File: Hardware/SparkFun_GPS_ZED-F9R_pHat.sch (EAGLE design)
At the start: 87 parts, among them J1 QWIIC_RIGHT_ANGLE, J2 RASPBERRYPI-40-PIN-GPIO_SMD_S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, J4 U.FL, U1 UBLOX_ZED_F9R, U2 HCPL-270L

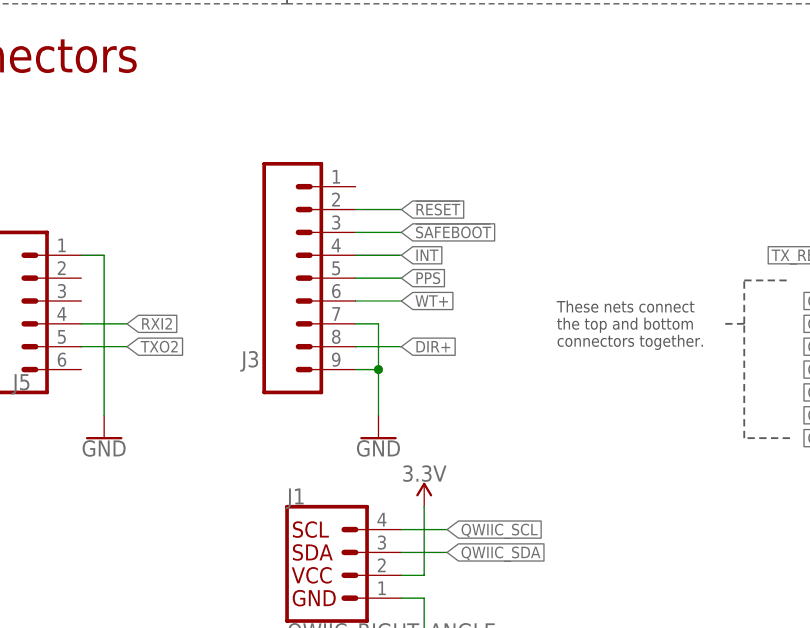
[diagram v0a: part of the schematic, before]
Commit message: Replaces 9-pin connector with 8-pin
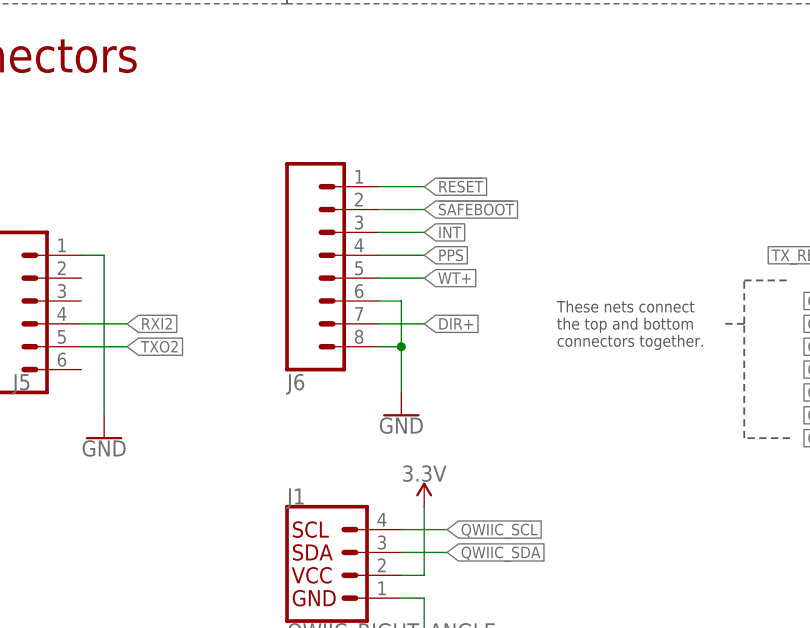
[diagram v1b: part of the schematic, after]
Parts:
- removed J3: (no value), SparkFun-Connectors:CONN_09NO_SILK
- added J6: (no value), SparkFun-Connectors:CONN_08NO_SILK_FEMALE_PTH
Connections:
- net !RESET: now also J6.1; no longer J3.2
- net !SAFEBOOT: now also J6.2; no longer J3.3
- net DIR+: now also J6.7; no longer J3.8
- net GND: now also J6.6, J6.8; no longer J3.7, J3.9
- net INT: now also J6.3; no longer J3.4
- net PPS: now also J6.4; no longer J3.5
- net WT+: now also J6.5; no longer J3.6
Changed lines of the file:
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@@
 <part name="GND3" library="SparkFun-PowerSymbols" deviceset="GND" device=""/>
 <part name="SUPPLY4" library="SparkFun-PowerSymbols" deviceset="3.3V" device=""/>
-<part name="J3" library="SparkFun-Connectors" deviceset="CONN_09" device="NO_SILK"/>
 <part name="J5" library="SparkFun-Connectors" deviceset="CONN_06" device="NO_SILK_NO_POP"/>
 <part name="GND5" library="SparkFun-PowerSymbols" deviceset="GND" device=""/>
@@
 <part name="GND15" library="SparkFun-PowerSymbols" deviceset="GND" device=""/>
 <part name="GND22" library="SparkFun-PowerSymbols" deviceset="GND" device=""/>
-<part name="GND23" library="SparkFun-PowerSymbols" deviceset="GND" device=""/>
+<part name="GND24" library="SparkFun-PowerSymbols" deviceset="GND" device=""/>
+<part name="J6" library="SparkFun-Connectors" deviceset="CONN_08" device="NO_SILK_FEMALE_PTH"/>
 </parts>
 <sheets>
@@
 <attribute name="VALUE" x="312.42" y="81.534" size="1.778" layer="96" align="bottom-center"/>
 </instance>
-<instance part="J3" gate="J1" x="294.64" y="104.14" smashed="yes" rot="MR180">
-<attribute name="VALUE" x="292.1" y="114.046" size="1.778" layer="96" font="vector" rot="MR180"/>
-<attribute name="NAME" x="292.1" y="96.012" size="1.778" layer="95" font="vector" rot="MR180"/>
-</instance>
 <instance part="J5" gate="G$1" x="269.24" y="101.6" smashed="yes" rot="MR180">
 <attribute name="VALUE" x="266.7" y="111.506" size="1.778" layer="96" font="vector" rot="MR180"/>
@@
 <attribute name="VALUE" x="340.36" y="210.566" size="1.778" layer="96" align="top-center"/>
 </instance>
-<instance part="GND23" gate="1" x="307.34" y="86.36" smashed="yes">
-<attribute name="VALUE" x="307.34" y="86.106" size="1.778" layer="96" align="top-center"/>
+<instance part="GND24" gate="1" x="309.88" y="88.9" smashed="yes">
+<attribute name="VALUE" x="309.88" y="88.646" size="1.778" layer="96" align="top-center"/>
+</instance>
+<instance part="J6" gate="G$1" x="302.26" y="106.68" smashed="yes" rot="MR180">
+<attribute name="VALUE" x="297.18" y="119.126" size="1.778" layer="96" font="vector" rot="MR180"/>
+<attribute name="NAME" x="297.18" y="93.472" size="1.778" layer="95" font="vector" rot="MR180"/>
 </instance>
 </instances>
@@
 </segment>
 <segment>
-<pinref part="J3" gate="J1" pin="9"/>
-<wire x1="304.8" y1="93.98" x2="307.34" y2="93.98" width="0.1524" layer="91"/>
-<pinref part="GND23" gate="1" pin="GND"/>
-<wire x1="307.34" y1="88.9" x2="307.34" y2="93.98" width="0.1524" layer="91"/>
-<pinref part="J3" gate="J1" pin="7"/>
-<wire x1="304.8" y1="99.06" x2="307.34" y2="99.06" width="0.1524" layer="91"/>
-<wire x1="307.34" y1="93.98" x2="307.34" y2="99.06" width="0.1524" layer="91"/>
-<junction x="307.34" y="93.98"/>
+<wire x1="307.34" y1="96.52" x2="309.88" y2="96.52" width="0.1524" layer="91"/>
+<pinref part="GND24" gate="1" pin="GND"/>
+<wire x1="309.88" y1="91.44" x2="309.88" y2="96.52" width="0.1524" layer="91"/>
+<wire x1="307.34" y1="101.6" x2="309.88" y2="101.6" width="0.1524" layer="91"/>
+<wire x1="309.88" y1="96.52" x2="309.88" y2="101.6" width="0.1524" layer="91"/>
+<junction x="309.88" y="96.52"/>
+<pinref part="J6" gate="G$1" pin="6"/>
+<pinref part="J6" gate="G$1" pin="8"/>
 </segment>
 </net>
@@
 </segment>
 <segment>
-<wire x1="304.8" y1="104.14" x2="309.88" y2="104.14" width="0.1524" layer="91"/>
-<label x="309.88" y="104.14" size="1.27" layer="95" font="vector" rot="MR180" xref="yes"/>
-<pinref part="J3" gate="J1" pin="5"/>
-</segment>
-<segment>
 <wire x1="111.76" y1="200.66" x2="114.3" y2="200.66" width="0.1524" layer="91"/>
 <label x="114.3" y="200.66" size="1.27" layer="95" font="vector" xref="yes"/>
 <pinref part="R24" gate="G$1" pin="2"/>
 </segment>
+<segment>
+<wire x1="307.34" y1="106.68" x2="312.42" y2="106.68" width="0.1524" layer="91"/>
+<label x="312.42" y="106.68" size="1.27" layer="95" font="vector" rot="MR180" xref="yes"/>
+<pinref part="J6" gate="G$1" pin="4"/>
+</segment>
 </net>
 <net name="!RESET" class="0">
@@
 </segment>
 <segment>
-<wire x1="304.8" y1="111.76" x2="309.88" y2="111.76" width="0.1524" layer="91"/>
-<label x="309.88" y="111.76" size="1.27" layer="95" font="vector" rot="MR180" xref="yes"/>
-<pinref part="J3" gate="J1" pin="2"/>
+<wire x1="307.34" y1="114.3" x2="312.42" y2="114.3" width="0.1524" layer="91"/>
+<label x="312.42" y="114.3" size="1.27" layer="95" font="vector" rot="MR180" xref="yes"/>
+<pinref part="J6" gate="G$1" pin="1"/>
 </segment>
 </net>
@@
 </segment>
 <segment>
-<wire x1="304.8" y1="106.68" x2="309.88" y2="106.68" width="0.1524" layer="91"/>
-<label x="309.88" y="106.68" size="1.27" layer="95" font="vector" rot="MR180" xref="yes"/>
-<pinref part="J3" gate="J1" pin="4"/>
+<wire x1="307.34" y1="109.22" x2="312.42" y2="109.22" width="0.1524" layer="91"/>
+<label x="312.42" y="109.22" size="1.27" layer="95" font="vector" rot="MR180" xref="yes"/>
+<pinref part="J6" gate="G$1" pin="3"/>
 </segment>
 </net>
@@
 <net name="!SAFEBOOT" class="0">
 <segment>
-<wire x1="304.8" y1="109.22" x2="309.88" y2="109.22" width="0.1524" layer="91"/>
-<label x="309.88" y="109.22" size="1.27" layer="95" font="vector" rot="MR180" xref="yes"/>
-<pinref part="J3" gate="J1" pin="3"/>
-</segment>
-<segment>
 <wire x1="111.76" y1="198.12" x2="114.3" y2="198.12" width="0.1524" layer="91"/>
 <label x="114.3" y="198.12" size="1.27" layer="95" font="vector" xref="yes"/>
 <pinref part="R25" gate="G$1" pin="2"/>
+</segment>
+<segment>
+<wire x1="307.34" y1="111.76" x2="312.42" y2="111.76" width="0.1524" layer="91"/>
+<label x="312.42" y="111.76" size="1.27" layer="95" font="vector" rot="MR180" xref="yes"/>
+<pinref part="J6" gate="G$1" pin="2"/>
 </segment>
 </net>
@@
 </segment>
 <segment>
-<pinref part="J3" gate="J1" pin="6"/>
-<wire x1="304.8" y1="101.6" x2="309.88" y2="101.6" width="0.1524" layer="91"/>
-<label x="309.88" y="101.6" size="1.27" layer="95" font="vector" xref="yes"/>
+<wire x1="307.34" y1="104.14" x2="312.42" y2="104.14" width="0.1524" layer="91"/>
+<label x="312.42" y="104.14" size="1.27" layer="95" font="vector" xref="yes"/>
+<pinref part="J6" gate="G$1" pin="5"/>
 </segment>
 </net>
@@
 </segment>
 <segment>
-<pinref part="J3" gate="J1" pin="8"/>
-<wire x1="304.8" y1="96.52" x2="309.88" y2="96.52" width="0.1524" layer="91"/>
-<label x="309.88" y="96.52" size="1.27" layer="95" xref="yes"/>
-</segment>
-</net>
+<wire x1="307.34" y1="99.06" x2="312.42" y2="99.06" width="0.1524" layer="91"/>
+<label x="312.42" y="99.06" size="1.27" layer="95" xref="yes"/>
+<pinref part="J6" gate="G$1" pin="7"/>
+</segment>
+</net>

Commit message: Renumbers parts, adds PROD_ID for new parts
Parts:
- removed C9: 0.1uF, SparkFun-Capacitors:0.1UF-0402-6.3V-10%-X7R
- removed J8: (no value), SparkFun-Connectors:USB_C_2-LAYER
- removed PPS, PWR: JUMPER-SMT_2_NC_TRACE_SILK, SparkFun-Jumpers:JUMPER-SMT_2_NC_TRACE_SILK
- added C4: 0.1uF, SparkFun-Capacitors:0.1UF-0402-6.3V-10%-X7R
- added J3: (no value), SparkFun-Connectors:CONN_06NO_SILK_NO_POP
- added JP5: JUMPER-SMT_2_NO_SILK, SparkFun-Jumpers:JUMPER-SMT_2_NO_SILK
- added JP6: JUMPER-SMT_3_2-NC_TRACE_SILK, SparkFun-Jumpers:JUMPER-SMT_3_2-NC_TRACE_SILK
- C1: value 47pF -> 1.0uF; device SparkFun-Capacitors:47PF-0402-25V-5%-X7R -> SparkFun-Capacitors:1.0UF-0402-16V-10%
- C2: value 1nF -> 1.0uF; device SparkFun-Capacitors:1.0NF/1000PF-0402-25V-10%-X7R -> SparkFun-Capacitors:1.0UF-0402-16V-10%
- C3: value 1.0uF -> 47pF; device SparkFun-Capacitors:1.0UF-0402-16V-10% -> SparkFun-Capacitors:47PF-0402-25V-5%-X7R
- C6: value 1.0uF -> 1nF; device SparkFun-Capacitors:1.0UF-0402-16V-10% -> SparkFun-Capacitors:1.0NF/1000PF-0402-25V-10%-X7R
- D1: value 0.5A/40V/420mV -> RED; device SparkFun-DiscreteSemi:DIODE-SCHOTTKY-PMEG4005EJ -> SparkFun-LED:LED-RED0603
- D2: value RED -> BLUE; device SparkFun-LED:LED-RED0603 -> SparkFun-LED:LED-BLUE0603
- D4: value PRTR5V0U2F -> BLUE; device SparkFun-IC-Power:PRTR5V0U2F -> SparkFun-LED:LED-BLUE0603
- D5: value BLUE -> 0.5A/40V/420mV; device SparkFun-LED:LED-BLUE0603 -> SparkFun-DiscreteSemi:DIODE-SCHOTTKY-PMEG4005EJ
- D6: value BLUE -> PRTR5V0U2F; device SparkFun-LED:LED-BLUE0603 -> SparkFun-IC-Power:PRTR5V0U2F
- J1: value QWIIC_RIGHT_ANGLE -> U.FL; device SparkFun-Connectors:QWIIC_CONNECTORJS-1MM -> SparkFun-Connectors:U.FL2PIN
- J2: value RASPBERRYPI-40-PIN-GPIO_SMD_STACK_NOHOLES_NOREF -> (none); device SparkFun-Connectors:RASPBERRYPI-40-PIN-GPIO_SMD_STACK_NOHOLES_NOREF -> SparkFun-Connectors:USB_C_2-LAYER
- J4: value U.FL -> (none); device SparkFun-Connectors:U.FL2PIN -> SparkFun-Connectors:CONN_08NO_SILK_FEMALE_PTH
- J5: value (none) -> QWIIC_RIGHT_ANGLE; device SparkFun-Connectors:CONN_06NO_SILK_NO_POP -> SparkFun-Connectors:QWIIC_CONNECTORJS-1MM
- J6: value (none) -> RASPBERRYPI-40-PIN-GPIO_SMD_STACK_NOHOLES_NOREF; device SparkFun-Connectors:CONN_08NO_SILK_FEMALE_PTH -> SparkFun-Connectors:RASPBERRYPI-40-PIN-GPIO_SMD_STACK_NOHOLES_NOREF
- JP1: value JUMPER-SMT_2_NO_SILK -> JUMPER-SMT_2_NC_TRACE_SILK; device SparkFun-Jumpers:JUMPER-SMT_2_NO_SILK -> SparkFun-Jumpers:JUMPER-SMT_2_NC_TRACE_SILK
- JP2: value JUMPER-SMT_3_2-NC_TRACE_SILK -> JUMPER-SMT_2_NC_TRACE_SILK; device SparkFun-Jumpers:JUMPER-SMT_3_2-NC_TRACE_SILK -> SparkFun-Jumpers:JUMPER-SMT_2_NC_TRACE_SILK
- LOGO1: value SFE_LOGO_NAME_FLAME.2_INCH -> QWIIC_LOGO_5MM; device SparkFun-Aesthetics:SFE_LOGO_NAME_FLAME.2_INCH -> SparkFun-Aesthetics:QWIIC_LOGO_5MM
- LOGO3: value QWIIC_LOGO_5MM -> SFE_LOGO_NAME_FLAME.2_INCH; device SparkFun-Aesthetics:QWIIC_LOGO_5MM -> SparkFun-Aesthetics:SFE_LOGO_NAME_FLAME.2_INCH
- R1: value 3.3k -> 100K; device SparkFun-Resistors:3.3KOHM-0603-1/10W-1% -> SparkFun-Resistors:100KOHM-0402-1/16W-1%
- R12: value 100K -> 33; device SparkFun-Resistors:100KOHM-0402-1/16W-1% -> SparkFun-Resistors:33OHM-0603-1/10W-1%
- R13, R14, R2, R8: value 1k -> 33; device SparkFun-Resistors:1KOHM-0603-1/10W-1% -> SparkFun-Resistors:33OHM-0603-1/10W-1%
- R15, R16: value 5.1k -> 33; device SparkFun-Resistors:5.1KOHM-0402-1/16W-1% -> SparkFun-Resistors:33OHM-0603-1/10W-1%
- R18, R23: value 33 -> 2.2k; device SparkFun-Resistors:33OHM-0603-1/10W-1% -> SparkFun-Resistors:2.2KOHM-0603-1/10W-1%
- R19, R20, R22: value 33 -> 1k; device SparkFun-Resistors:33OHM-0603-1/10W-1% -> SparkFun-Resistors:1KOHM-0603-1/10W-1%
- R21: value 3.3k -> 1k; device SparkFun-Resistors:3.3KOHM-0603-1/10W-1% -> SparkFun-Resistors:1KOHM-0603-1/10W-1%
- R24, R25: value 33 -> 5.1k; device SparkFun-Resistors:33OHM-0603-1/10W-1% -> SparkFun-Resistors:5.1KOHM-0402-1/16W-1%
- R26, R29: value 33 -> 3.3k; device SparkFun-Resistors:33OHM-0603-1/10W-1% -> SparkFun-Resistors:3.3KOHM-0603-1/10W-1%
- R27, R28: value 33 -> 27; device SparkFun-Resistors:33OHM-0603-1/10W-1% -> SparkFun-Resistors:27OHM-0603-1/10W-1%
- R3, R4: value 2.2k -> 33; device SparkFun-Resistors:2.2KOHM-0603-1/10W-1% -> SparkFun-Resistors:33OHM-0603-1/10W-1%
- R30: value 470 -> 3.3k; device SparkFun-Resistors:470OHM-0603-1/10W-1% -> SparkFun-Resistors:3.3KOHM-0603-1/10W-1%
- R31: value 3.3k -> 910; device SparkFun-Resistors:3.3KOHM-0603-1/10W-1% -> classified:910OHM-0603-1/10W-5%
- R32: value 470 -> 910; device SparkFun-Resistors:470OHM-0603-1/10W-1% -> classified:910OHM-0603-1/10W-5%
- R33, R34: value 910 -> 470; device classified:910OHM-0603-1/10W-5% -> SparkFun-Resistors:470OHM-0603-1/10W-1%
- R6, R7: value 27 -> 33; device SparkFun-Resistors:27OHM-0603-1/10W-1% -> SparkFun-Resistors:33OHM-0603-1/10W-1%
- U2: value HCPL-270L -> HCPL-073L; device classified:HCPL-270L -> classified:HCPL-073L
- renumbered B1 to BT1, FD10 to FD2, FD11 to FD3, FD12 to FD4, FD9 to FD1, FRAME2 to FRAME1, GEO_STAT to JP4, H10 to H1, H11 to H3, H12 to H4, H9 to H2, RTK to JP3, U$30 to U3, U$31 to U4
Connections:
- net !RESET: now also J4.1, R5.2; no longer J6.1, R9.2
- net !SAFEBOOT: now also J4.2, R17.2; no longer J6.2, R25.2
- net 3.3V: now also C1.1, C2.1, C4.1, D5.A, J5.2, J6.3.3V, JP6.2, R1.2, R31.2, R32.2; no longer C3.1, C6.1, C9.1, D2.A, J1.2, J2.3.3V, JP2.2, R12.2, R33.2, R34.2
- net CE1: now also J6.CE1; no longer J2.CE1
- net DIR+: now also J4.7, R30.1; no longer J6.7, R31.1
- net DIR_IN: now also R33.2; no longer R32.2
- net DIR_OUT: now also R4.1; no longer R29.1
- net DIR_SCHMITT: now also R32.1; no longer R34.1
- net DMINUS: now also R28.2; no longer R7.2
- net DPLUS: now also R27.2; no longer R6.2
- net D_SEL: now also JP5.1; no longer JP1.1
- net GEOF_STAT: now also D4.A, R14.2; no longer D3.A, R22.2
- net GND: now also C4.2, D6.2, J1.GND, J3.1, J4.6, J4.8, J6.GND, JP1.1, JP2.1, JP5.2, R1.1, R24.1, R25.1; no longer C9.2, D4.2, J1.1, J4.GND, J6.6, J6.8, J8.GND, JP1.2, PPS.1, PWR.1, R12.1, R15.1, R16.1
- net GP12: now also J6.GP12; no longer J2.GP12
- net GP13: now also J6.GP13; no longer J2.GP13
- net GP16: now also J6.GP16; no longer J2.GP16
- net GP17: now also J6.GP17; no longer J2.GP17
- net GP18: now also J6.GP18#; no longer J2.GP18#
- net GP19: now also J6.GP19; no longer J2.GP19
- net GP20: now also J6.GP20; no longer J2.GP20
- net GP21: now also J6.GP21; no longer J2.GP21
- net GP22: now also J6.GP22; no longer J2.GP22
- net GP23: now also J6.GP23; no longer J2.GP23
- net GP24: now also J6.GP24; no longer J2.GP24
- net GP25: now also J6.GP25; no longer J2.GP25
- net GP26: now also J6.GP26; no longer J2.GP26
- net GP27: now also J6.GP27; no longer J2.GP27
- net GP4: now also J6.GP4; no longer J2.GP4
- net GP6: now also J6.GP6; no longer J2.GP6
- net ID_SC: now also J6.ID_SC; no longer J2.ID_SC
- net ID_SD: now also J6.ID_SD; no longer J2.ID_SD
- net INT: now also J4.3, R6.2; no longer J6.3, R10.2
- net N$1: now also JP6.1, R23.2; no longer JP2.1, R3.2
- net N$10: now also D6.5, J2.VBUS; no longer D4.5, J8.VBUS
- net N$11: now also D6.1, J2.D-; no longer D4.1, J8.D-
- net N$12: now also J2.CC2, R24.2; no longer J8.CC2, R15.2
- net N$13: now also R5.1; no longer R9.1
- net N$14: now also R6.1; no longer R10.1
- net N$15: now also R7.1; no longer R11.1
- net N$16: now also R22.1; no longer R8.1
- net N$17: now also D4.C, R22.2; no longer D3.C, R8.2
- net N$18: now also J2.CC1, R25.2; no longer J8.CC1, R16.2
- net N$19: now also R8.1; no longer R17.1
- net N$2: now also D5.C, R26.2; no longer D1.C, R1.2
- net N$20: now also R9.1; no longer R18.1
- net N$21: now also R10.1; no longer R19.1
- net N$22: now also R21.1; no longer R14.1
- net N$23: now also JP2.2, R20.1; no longer PPS.2, R13.1
- net N$24: now also D2.C, R20.2; no longer D5.C, R13.2
- net N$25: now also D3.C, R21.2; no longer D6.C, R14.2
- net N$26: now also R11.1; no longer R20.1
- net N$27: now also C6.1, D8.C, R29.2, R34.1; no longer C5.1, D7.C, R21.2, R30.1
- net N$28: now also R14.1; no longer R22.1
- net N$29: now also R15.1; no longer R23.1
- net N$3: now also JP6.3, R18.2; no longer JP2.3, R4.2
- net N$30: now also R16.1; no longer R24.1
- net N$31: now also R17.1; no longer R25.1
- net N$32: now also R12.1; no longer R26.1
- net N$33: now also R13.1; no longer R27.1
- net N$34: now also R3.2; no longer R28.2
- net N$35: now also R4.2; no longer R29.2
- net N$36: now also C5.1, D7.C, R30.2, R33.1; no longer C2.1, D8.C, R31.2, R32.1
- net N$4: now also D1.C, R19.2; no longer D2.C, R2.2
- net N$5: now also C3.1, R2.1; no longer C1.1, R5.1
- net N$6: now also D6.6, R28.1; no longer D4.6, R7.1
- net N$7: now also D6.4, R27.1; no longer D4.4, R6.1
- net N$8: now also JP1.2, R19.1; no longer PWR.2, R2.1
- net N$9: now also D6.3, J2.D+; no longer D4.3, J8.D+
- net PPS: now also D2.A, J4.4, R16.2; no longer D5.A, J6.4, R24.2
- net QWIIC_SCL: now also J5.4, J6.SCL, R18.1; no longer J1.4, J2.SCL, R4.1
- net QWIIC_SDA: now also J5.3, J6.SDA, R23.1; no longer J1.3, J2.SDA, R3.1
- net RF_IN: now also J1.SIGNAL; no longer J4.SIGNAL
- net RTK_STAT: now also D3.A, R15.2; no longer D6.A, R23.2
- net RXI/MOSI: now also J6.MOSI, J6.TXO, R11.2; no longer J2.MOSI, J2.TXO, R20.2
- net RXI2: now also J3.4, R13.2; no longer J5.4, R27.2
- net SCL/CLK: now also J6.SCLK, R8.2; no longer J2.SCLK, R17.2
- net SDA/!CS: now also J6.CE0, R7.2; no longer J2.CE0, R11.2
- net SHIELD: now also J2.SHLD; no longer J8.SHLD
- net TXO/MISO: now also J6.MISO, J6.RXI, R10.2; no longer J2.MISO, J2.RXI, R19.2
- net TXO2: now also J3.5, R12.2; no longer J5.5, R26.2
- net TX_READY: now also J6.GP5, R9.2; no longer J2.GP5, R18.2
- net V_BATT: now also R26.1; no longer R1.1
- net V_RF: now also R2.2; no longer R5.2
- net WT+: now also J4.5, R29.1; no longer J6.5, R21.1
- net WT_IN: now also R34.2; no longer R30.2
- net WT_OUT: now also R3.1; no longer R28.1
- net WT_SCHMITT: now also R31.1; no longer R33.1
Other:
- moved on the sheet: C1, C2, C3, C5, C6, C7, C8, D2, D3, D7, D8, R1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
